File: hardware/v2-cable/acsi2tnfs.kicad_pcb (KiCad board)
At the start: 2 copper layers, 97.1 x 53.8 mm, 23 parts, among them J1 To ACSI, J2 ACSI pass-through, J3 To SD card, SW1 SW_Prev, U1 SN74LVC245APW, U2 SN74LVC245APW, U3 SN74LS07

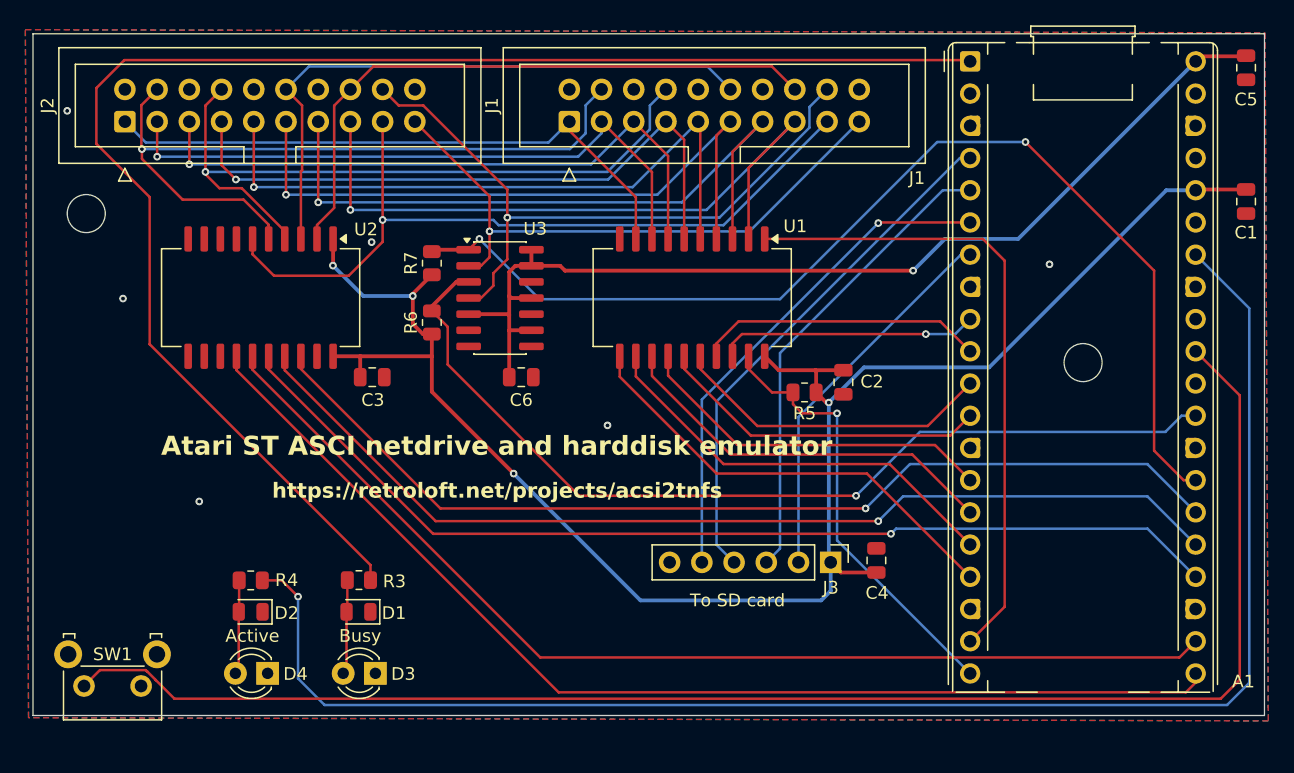
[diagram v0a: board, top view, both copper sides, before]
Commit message: hardware/v2-cable: TF-01A micro SD socket on the board, new layout
The SD module is replaced by a TF-01A push-push socket (LCSC C91145) that
sticks out 2.4 mm over the front edge, flush with the case front. Button,
leds and mounting holes moved to fit the 3D-printed case.

Co-Authored-By: Claude Opus 5.5 <noreply@anthropic.com>
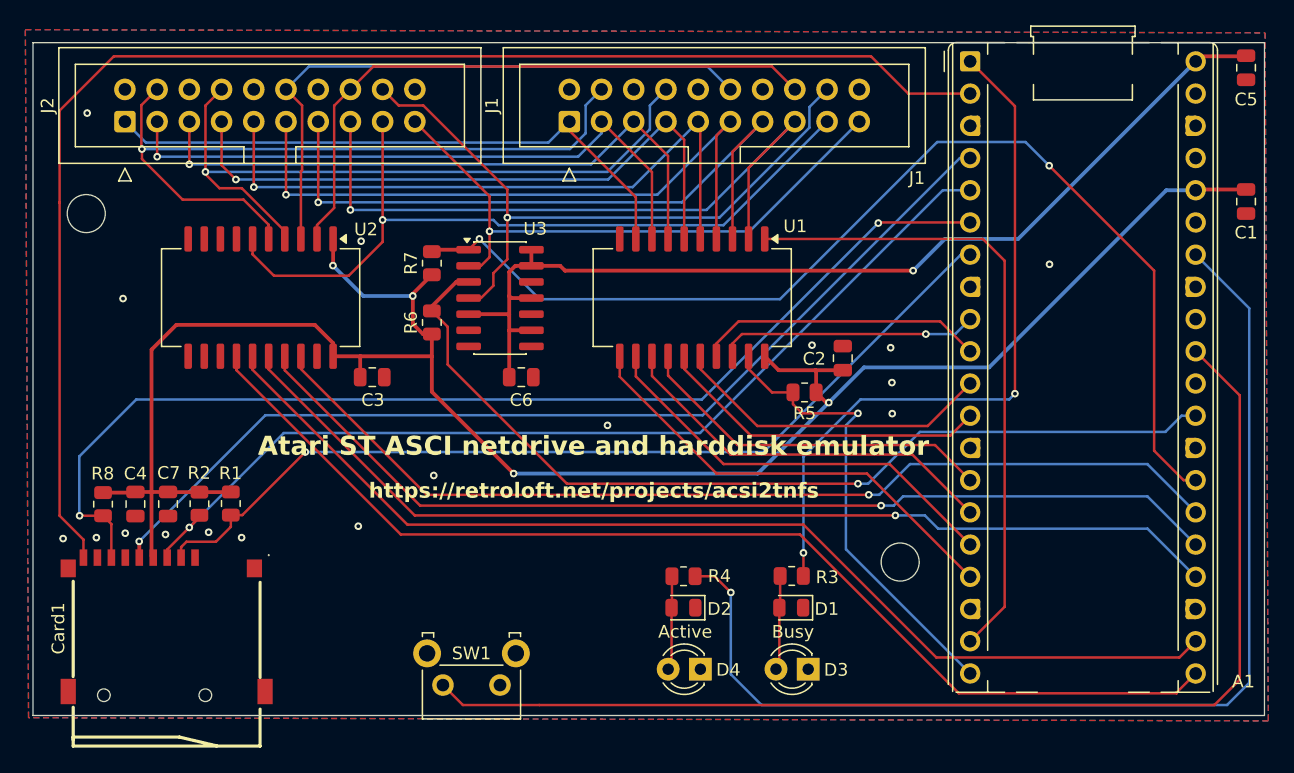
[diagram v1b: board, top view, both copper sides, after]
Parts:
- removed J3: To SD card, Connector_PinHeader_2.54mm:PinHeader_1x06_P2.54mm_Vertical
- added C7: 10uF, Capacitor_SMD:C_0805_2012Metric, F.Cu at (109.8, 98.4)
- added Card1: TF-01A, Micro SD card:TF-SMD_TF-01A, F.Cu at (109.6, 107.9)
- added R1: 10K, Resistor_SMD:R_0805_2012Metric, F.Cu at (114.7, 98.4)
- added R2: 10K, Resistor_SMD:R_0805_2012Metric, F.Cu at (112.2, 98.4)
- added R8: 10K, Resistor_SMD:R_0805_2012Metric, F.Cu at (104.6, 98.4)
- C1, C5: value 10 µF -> 10 uF
- C2, C3, C4, C6: value 100n -> 100nF
- R3, R4: value 330 -> 330R
- moved C4 58.6 mm to (107.2, 98.4), turned to -90 degrees
- moved R3 34.1 mm to (158.9, 104.1)
- moved D3 34.1 mm to (160.2, 111.4)
- moved D4 34.1 mm to (151.7, 111.4)
- moved R4 34.1 mm to (150.4, 104.1)
- moved D1 34.1 mm to (158.9, 106.6)
- moved D2 34.1 mm to (150.4, 106.6)
- moved SW1 28.3 mm to (135.9, 112.7)
- moved C2 1.90 mm to (162.9, 86.9), turned to 90 degrees
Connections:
- A1 pad 2: unconnected-(A1-GPIO1-Pad2) -> CD
- A1 pad 4: CLK -> SCLK
- A1 pad 7: CS -> SD_CS
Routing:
- net CD: track 0.00 -> 110.8 mm
- net SCLK: track 0.00 -> 79.3 mm, vias 0 -> 1
- net SD_CS: track 0.00 -> 73.2 mm, vias 0 -> 1
- net POWER_LED: track 117.6 -> 55.9 mm, vias 0 -> 2
- net MISO: track 39.8 -> 88.0 mm, vias 1 -> 2
- net CLK: track 41.2 -> 0.00 mm
- net MOSI: track 37.3 -> 77.0 mm, vias 0 -> 1
- net STATUS_LED: track 121.9 -> 87.9 mm
- net CS: track 30.3 -> 0.00 mm
- net BUTTON: track 120.5 -> 91.6 mm
- net +3.3V: track 136.7 -> 158.8 mm
- net /OE: track 34.8 -> 36.6 mm
- net A1_3V3: track 80.2 -> 79.2 mm
- net R/W_3V3: track 79.1 -> 78.2 mm
- net Net-(A1-GPIO22): track 74.7 -> 73.9 mm
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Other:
- board size 97.1 x 53.8 mm -> 97.1 x 53.1 mm

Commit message: hardware/v2-cable: drop unused library files, update schema.pdf
The TF-01A symbol is stored in the schematic and the 2x10 pin header
footprint is not used. Card1 now uses the footprint from the project
library, so the project no longer needs a global "Micro SD card" library.

Co-Authored-By: Claude Opus 5.5 <noreply@anthropic.com>
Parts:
- Card1: footprint Micro SD card:TF-SMD_TF-01A -> Library:TF-SMD_TF-01A
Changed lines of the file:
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@@
 		)
 	)
-	(footprint "Micro SD card:TF-SMD_TF-01A"
+	(footprint "Library:TF-SMD_TF-01A"
 		(layer "F.Cu")
 		(at 109.64 107.905)

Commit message: hardware: U1/U2 are 74LVC245ADW, silkscreen says ACSI
Both boards: the value of U1/U2 matches the SOIC-20W footprint, the
silkscreen text reads ACSI instead of ASCI, and a stray text outside the
v2 board is gone. schema.pdf and the 3D views updated.

Co-Authored-By: Claude Opus 5.5 <noreply@anthropic.com>
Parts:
- U1, U2: value SN74LVC245APW -> 74LVC245ADW
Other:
- board text added: "Atari ST ACSI netdrive and harddisk emulator"
- board text removed: "Atari ST ASCI netdrive and harddisk emulator"
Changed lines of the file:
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@@
 			)
 		)
-		(property "Value" "SN74LVC245APW"
+		(property "Value" "74LVC245ADW"
 			(at 0 8.66 90)
 			(layer "F.Fab")
@@
 			)
 		)
-		(property "Value" "SN74LVC245APW"
+		(property "Value" "74LVC245ADW"
 			(at 0 8.66 90)
 			(layer "F.Fab")
@@
 		)
 	)
-	(gr_text "Atari ST ASCI netdrive and harddisk emulator"
+	(gr_text "Atari ST ACSI netdrive and harddisk emulator"
 		(at 116.825 94.7 0)
 		(layer "F.SilkS")

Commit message: hardware: D1 yellow, D2 blue, both on 470 ohm
R3 and R4 are 470 ohm in both boards; the led values name the colour
(v2-cable: D3 yellow, D4 blue as well). schema.pdf and the parts list
updated.

Co-Authored-By: Claude Opus 5.5 <noreply@anthropic.com>
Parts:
- D1, D3: value LED -> LED yellow
- D2, D4: value LED -> LED blue
- R3, R4: value 330R -> 470
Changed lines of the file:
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@@
 			)
 		)
-		(property "Value" "330R"
+		(property "Value" "470"
 			(at -3.269577 -0.02116 0)
 			(layer "F.Fab")
@@
 			)
 		)
-		(property "Value" "LED"
+		(property "Value" "LED yellow"
 			(at 3.2625 3.9 0)
 			(layer "F.Fab")
@@
 			)
 		)
-		(property "Value" "LED"
+		(property "Value" "LED yellow"
 			(at 1.27 2.96 0)
 			(layer "F.Fab")
@@
 			)
 		)
-		(property "Value" "330R"
+		(property "Value" "470"
 			(at -3.3 0 0)
 			(layer "F.Fab")
@@
 			)
 		)
-		(property "Value" "LED"
+		(property "Value" "LED blue"
 			(at 3.2625 3.8 0)
 			(layer "F.Fab")
@@
 			)
 		)
-		(property "Value" "LED"
+		(property "Value" "LED blue"
 			(at 1.27 2.96 0)
 			(layer "F.Fab")
